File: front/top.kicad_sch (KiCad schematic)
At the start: 1 part, among them U1 LSM6DSO32TR

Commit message: start adding components
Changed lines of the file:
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@@
 	(symbol
 		(lib_id "New_Library:LSM6DSO32TR")
-		(at 121.92 71.12 0)
+		(at 129.54 86.36 0)
 		(unit 1)
 		(exclude_from_sim no)
@@
 		(fields_autoplaced yes)
 		(property "Reference" "U1"
-			(at 121.92 50.8 0)
+			(at 129.54 66.04 0)
 			(effects
 				(font
@@
 		)
 		(property "Value" "LSM6DSO32TR"
-			(at 121.92 53.34 0)
+			(at 129.54 68.58 0)
 			(effects
 				(font
@@
 		)
 		(property "Footprint" "Library:XDCR_LSM6DSO32TR"
-			(at 121.92 71.12 0)
+			(at 129.54 86.36 0)
 			(effects
 				(font
@@
 		)
 		(property "Datasheet" ""
-			(at 121.92 71.12 0)
+			(at 129.54 86.36 0)
 			(effects
 				(font
@@
 		)
 		(property "Description" ""
-			(at 121.92 71.12 0)
+			(at 129.54 86.36 0)
 			(effects
 				(font
@@
 		)
 		(property "PARTREV" "1"
-			(at 121.92 71.12 0)
+			(at 129.54 86.36 0)
 			(effects
 				(font
@@
 		)
 		(property "STANDARD" "Manufacturer Recommendations"
-			(at 121.92 71.12 0)
+			(at 129.54 86.36 0)
 			(effects
 				(font
@@
 		)
 		(property "MAXIMUM_PACKAGE_HEIGHT" "0.86mm"
-			(at 121.92 71.12 0)
+			(at 129.54 86.36 0)
 			(effects
 				(font
@@
 		)
 		(property "MANUFACTURER" "STMicroelectronics"
-			(at 121.92 71.12 0)
+			(at 129.54 86.36 0)
 			(effects
 				(font
@@
 			)
 		)
-		(pin "3"
+		(pin "8"
 		)
-		(pin "11"
-		)
-		(pin "4"
+		(pin "7"
 		)
 		(pin "2"
@@
 		(pin "10"
 		)
-		(pin "8"
+		(pin "12"
+		)
+		(pin "3"
+		)
+		(pin "4"
+		)
+		(pin "1"
+		)
+		(pin "5"
+		)
+		(pin "11"
+		)
+		(pin "6"
 		)
 		(pin "9"
 		)
-		(pin "6"
-		)
-		(pin "12"
-		)
-		(pin "7"
-		)
-		(pin "5"
+		(pin "14"
 		)
 		(pin "13"
 		)
-		(pin "14"
-		)
-		(pin "1"
-		)
 		(instances
-			(project ""
-				(path "/17e03e84-549e-45f3-83eb-0d4a5f3096f9"
+			(project "front"
+				(path "/508f986b-6f1b-4c39-bd57-bae69573a4e7/843258f1-78c3-468e-9a1f-11cdaf4e9c54"
 					(reference "U1")
 					(unit 1)
@@
 		)
 	)
-	(sheet_instances
-		(path "/"
-			(page "1")
-		)
-	)
-	(embedded_fonts no)
 )

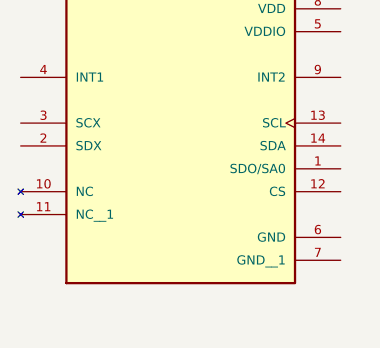
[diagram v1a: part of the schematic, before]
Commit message: add some traces
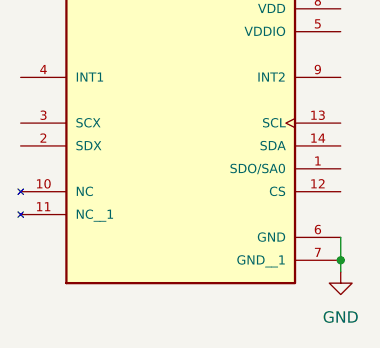
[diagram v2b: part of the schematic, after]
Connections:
- net GND: now reaches U1.6 (GND)
- net GND: now also U1.7 (GND__1)
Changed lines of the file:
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@@
 	(generator_version "9.0")
 	(paper "A4")
+	(junction
+		(at 147.32 101.6)
+		(diameter 0)
+		(color 0 0 0 0)
+	)
+	(wire
+		(pts
+			(xy 147.32 99.06) (xy 147.32 101.6)
+		)
+		(stroke
+			(width 0)
+			(type default)
+		)
+	)
+	(wire
+		(pts
+			(xy 147.32 101.6) (xy 147.32 102.87)
+		)
+		(stroke
+			(width 0)
+			(type default)
+		)
+	)
+	(symbol
+		(lib_id "power:GND")
+		(at 147.32 102.87 0)
+		(unit 1)
+		(exclude_from_sim no)
+		(in_bom yes)
+		(on_board yes)
+		(dnp no)
+		(fields_autoplaced yes)
+		(property "Reference" "#PWR01"
+			(at 147.32 109.22 0)
+			(effects
+				(font
+					(size 1.27 1.27)
+				)
+				(hide yes)
+			)
+		)
+		(property "Value" "GND"
+			(at 147.32 107.95 0)
+			(effects
+				(font
+					(size 1.27 1.27)
+				)
+			)
+		)
+		(property "Footprint" ""
+			(at 147.32 102.87 0)
+			(effects
+				(font
+					(size 1.27 1.27)
+				)
+				(hide yes)
+			)
+		)
+		(property "Datasheet" ""
+			(at 147.32 102.87 0)
+			(effects
+				(font
+					(size 1.27 1.27)
+				)
+				(hide yes)
+			)
+		)
+		(property "Description" "Power symbol creates a global label with name \"GND\" , ground"
+			(at 147.32 102.87 0)
+			(effects
+				(font
+					(size 1.27 1.27)
+				)
+				(hide yes)
+			)
+		)
+		(pin "1"
+		)
+		(instances
+			(project ""
+				(path "/508f986b-6f1b-4c39-bd57-bae69573a4e7/843258f1-78c3-468e-9a1f-11cdaf4e9c54"
+					(reference "#PWR01")
+					(unit 1)
+				)
+			)
+		)
+	)
 	(symbol
 		(lib_id "New_Library:LSM6DSO32TR")

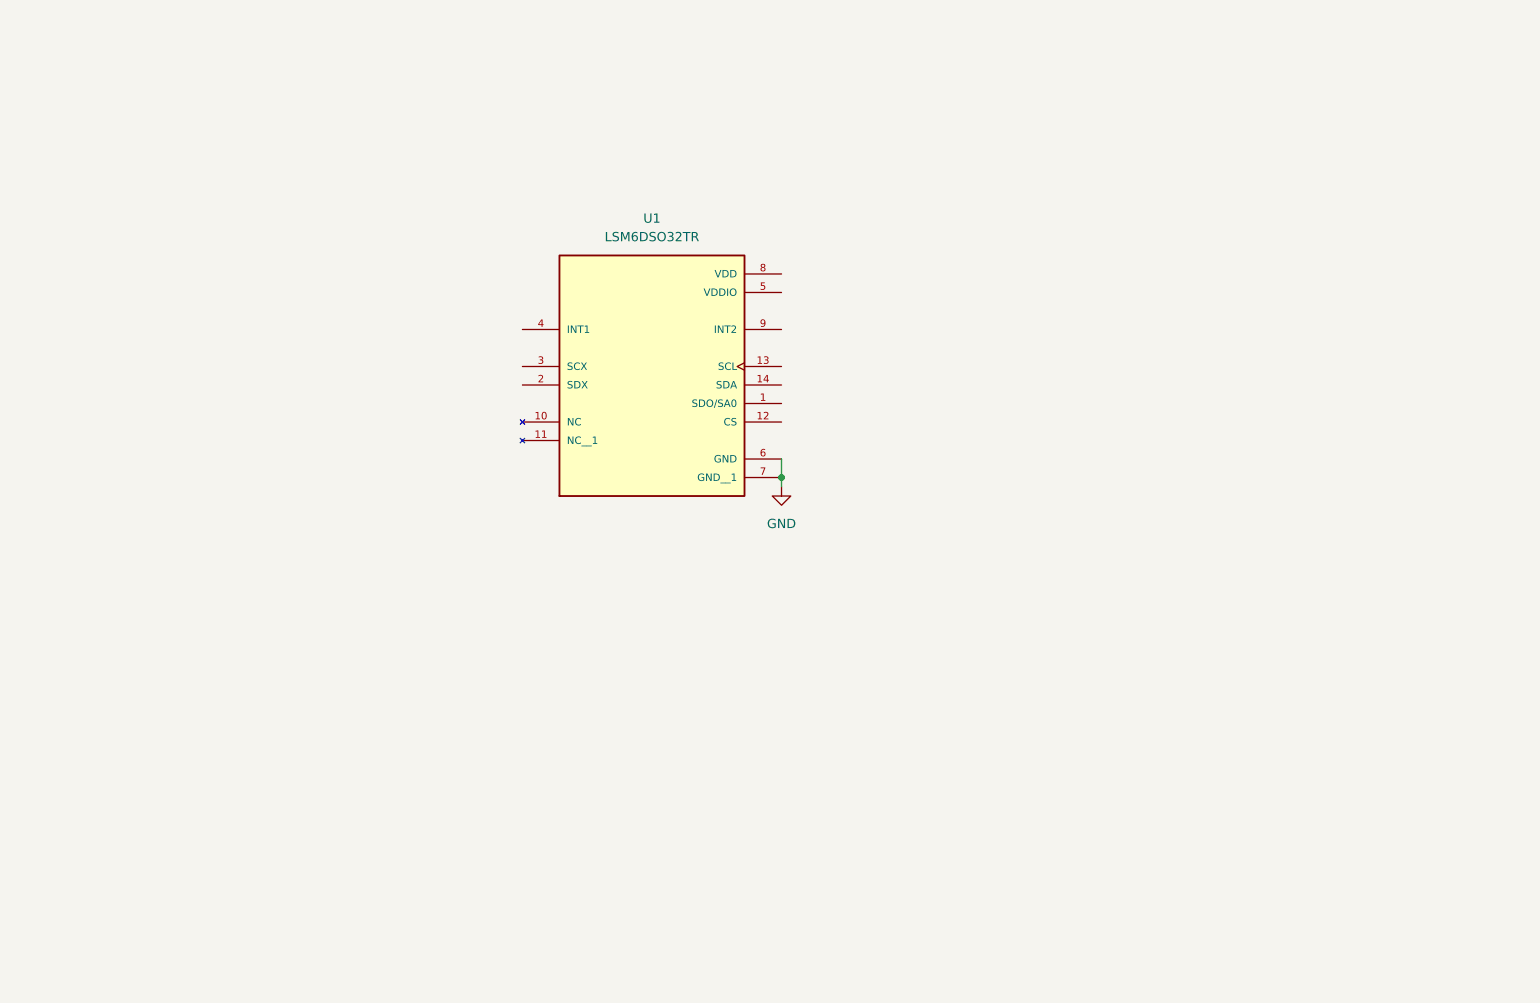
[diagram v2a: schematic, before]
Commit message: undo panelizing
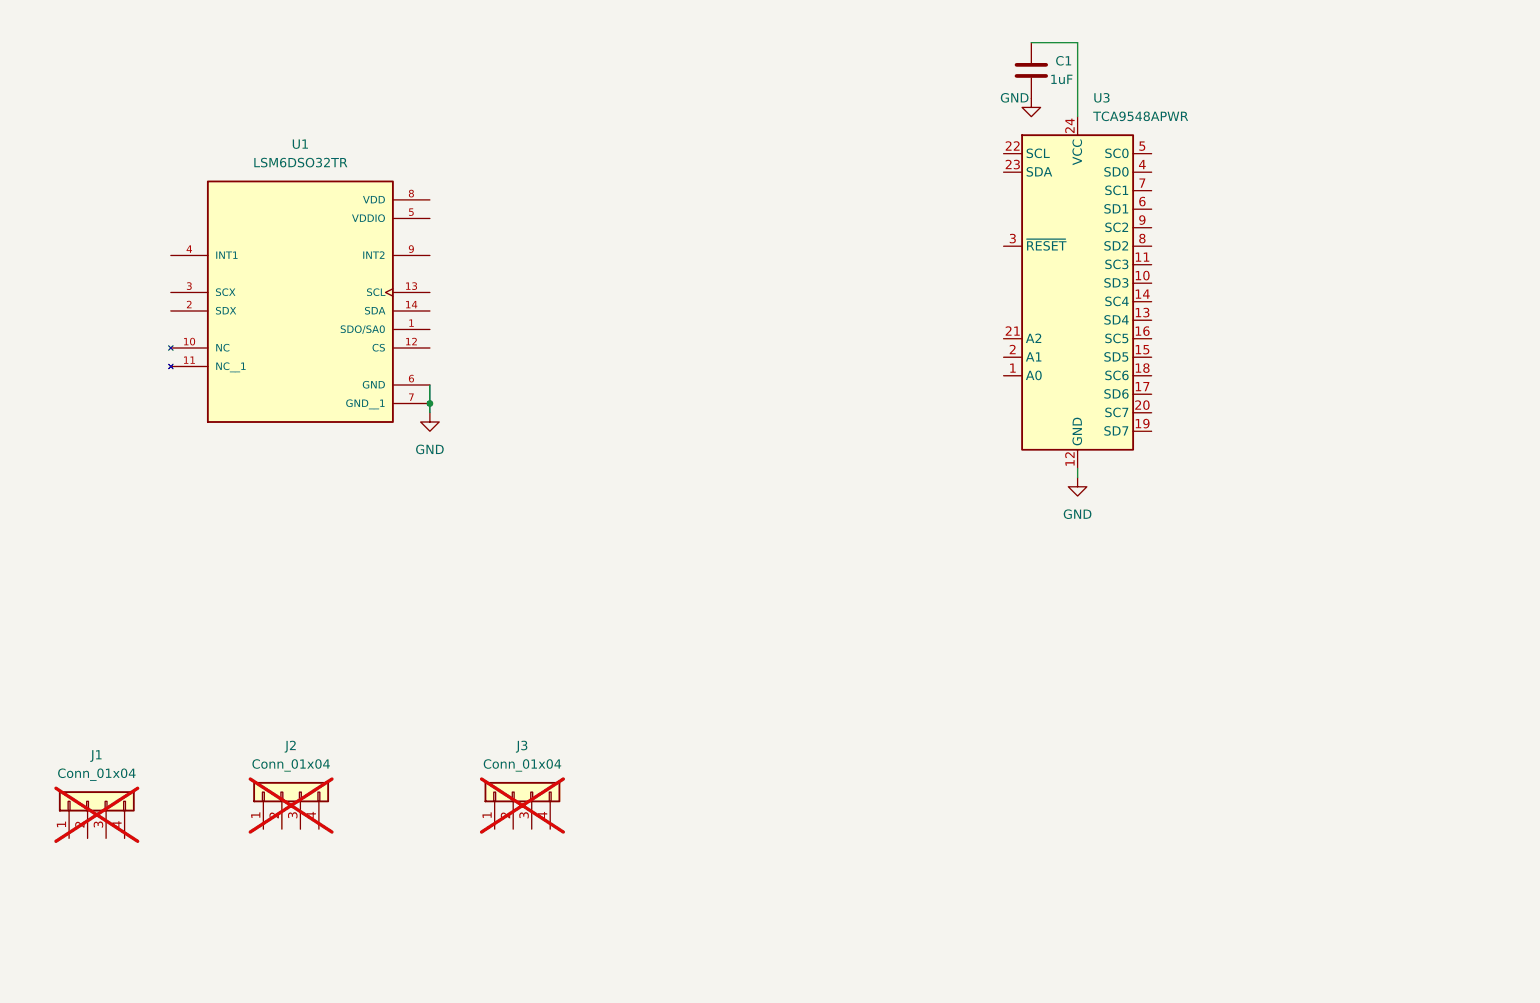
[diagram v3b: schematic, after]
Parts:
- added C1: 1uF, Capacitor_SMD:C_0603_1608Metric, symbol Device:C
- added J1, J2, J3: Conn_01x04, Connector_PinHeader_2.54mm:PinHeader_1x04_P2.54mm_Vertical, symbol Connector_Generic:Conn_01x04
- added U3: TCA9548APWR, Package_SO:TSSOP-24_4.4x7.8mm_P0.65mm, symbol Interface_Expansion:TCA9548APWR
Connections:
- net GND: now also C1.2, U3.12 (GND)
- new net: C1.1, U3.24 (VCC)
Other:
- moved on the sheet: U1

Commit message: add more components
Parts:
- removed U3: TCA9548APWR, Package_SO:TSSOP-24_4.4x7.8mm_P0.65mm, symbol Interface_Expansion:TCA9548APWR
- added C5, C6, C7: 100n, Capacitor_SMD:C_0603_1608Metric, symbol Device:C
- added NT1: NetTie_3, Jumper:SolderJumper-3_P1.3mm_Bridged12_RoundedPad1.0x1.5mm, symbol Device:NetTie_3
- added U3: PCA9848PWJ, Library:TSSOP24_SOT355-1_NEX_NXP, symbol New_Library:PCA9848PWJ
- C1: value 1uF -> 100n
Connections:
- net GND: now also U1.1 (SDO/SA0), U1.2 (SDX), U1.3 (SCX), C5.2, C6.2, C7.2, NT1.1, U3.12 (VSS)
- net 1.8v: now reaches C1.1
- net 1.8v: now also U1.12 (CS), U1.5 (VDDIO), U1.8 (VDD), C5.1, C6.1, C7.1, NT1.3, U3.1 (VDD1), U3.2 (A0), U3.24 (VDD2), U3.3 (*RESET)
- net scimu: now reaches U1.13 (SCL)
- net scimu: now also U3.14 (SC4)
- net sdimu: now reaches U1.14 (SDA)
- net sdimu: now also U3.13 (SD4)
- new net: NT1.2, U3.21 (A1)
- new net sc1: U3.7 (SC1)
- new net sc2: U3.9 (SC2)
- new net sc3: U3.11 (SC3)
- new net scl: U3.22 (SCL)
- new net sd1: U3.6 (SD1)
- new net sd2: U3.8 (SD2)
- new net sd3: U3.10 (SD3)
- new net sda: U3.23 (SDA)
- no-connect marks 0 -> 10
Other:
- moved on the sheet: C1, U1

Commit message: begin layout
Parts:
- removed C6, C7: 100n, Capacitor_SMD:C_0603_1608Metric, symbol Device:C
- removed U1: LSM6DSO32TR, Library:XDCR_LSM6DSO32TR, symbol New_Library:LSM6DSO32TR
- added J5: Conn_01x06_Pin, Connector_PinSocket_2.54mm:PinSocket_1x06_P2.54mm_Vertical, symbol Connector:Conn_01x06_Pin
- added NT0: NetTie_3, Jumper:SolderJumper-3_P1.3mm_Bridged12_RoundedPad1.0x1.5mm, symbol Device:NetTie_3
- J1, J2, J3: value Conn_01x04 -> Conn_01x05; footprint Connector_PinHeader_2.54mm:PinHeader_1x04_P2.54mm_Vertical -> Connector_PinHeader_2.54mm:PinHeader_1x05_P2.54mm_Vertical; symbol Connector_Generic:Conn_01x04 -> Connector:Conn_01x05_Pin; now in the parts list
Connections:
- net 1.8v: now also J1.5 (Pin_5), J2.5 (Pin_5), J3.5 (Pin_5), NT0.3; no longer U3.2 (A0)
- net GND: now also J1.1 (Pin_1), J2.1 (Pin_1), J3.1 (Pin_1), NT0.1
- net 3.3v: now reaches J3.2 (Pin_2)
- net 3.3v: now also J1.2 (Pin_2), J2.2 (Pin_2)
- net sc_vl: now reaches J3.3 (Pin_3)
- net sc_vl: now also J1.3 (Pin_3), J2.3 (Pin_3)
- net sd_vl: now reaches J3.4 (Pin_4)
- net sd_vl: now also J1.4 (Pin_4), J2.4 (Pin_4)
- net scimu: no longer names the net of U3.14 (SC4)
- net sdimu: no longer names the net of U3.13 (SD4)
- new net: NT0.2, U3.2 (A0)
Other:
- moved on the sheet: C1, C5, NT1, U3

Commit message: layout front top
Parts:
- removed C1: 100n, Capacitor_SMD:C_0603_1608Metric, symbol Device:C
- removed NT0: NetTie_3, Jumper:SolderJumper-3_P1.3mm_Bridged12_RoundedPad1.0x1.5mm, symbol Device:NetTie_3
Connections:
- net sd_vl is gone; now on net 3.3v: J1.4 (Pin_4), J2.4 (Pin_4), J3.4 (Pin_4)
- net 1.8v: now also J1.1 (Pin_1), J2.1 (Pin_1), J3.1 (Pin_1), J5.1 (Pin_1), U3.2 (A0); no longer J1.5 (Pin_5), J2.5 (Pin_5), J3.5 (Pin_5)
- net 3.3v: now also J5.4 (Pin_4); no longer J1.2 (Pin_2), J2.2 (Pin_2), J3.2 (Pin_2)
- net GND: now also J1.5 (Pin_5), J2.5 (Pin_5), J3.5 (Pin_5), J5.5 (Pin_5), J5.6 (Pin_6); no longer J1.1 (Pin_1), J2.1 (Pin_1), J3.1 (Pin_1)
- net sc1: now also J1.3 (Pin_3)
- net sc2: now also J2.3 (Pin_3)
- net sc3: now also J3.3 (Pin_3), U3.14 (SC4); no longer U3.11 (SC3)
- net scl: now also J5.2 (Pin_2)
- net sd1: now also J1.2 (Pin_2)
- net sd2: now also J2.2 (Pin_2)
- net sd3: now also J3.2 (Pin_2), U3.13 (SD4); no longer U3.10 (SD3)
- net sda: now also J5.3 (Pin_3)
- removed net sc_vl: J1.3 (Pin_3), J2.3 (Pin_3), J3.3 (Pin_3)
